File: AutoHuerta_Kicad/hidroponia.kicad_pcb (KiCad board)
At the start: 2 copper layers, 1 part

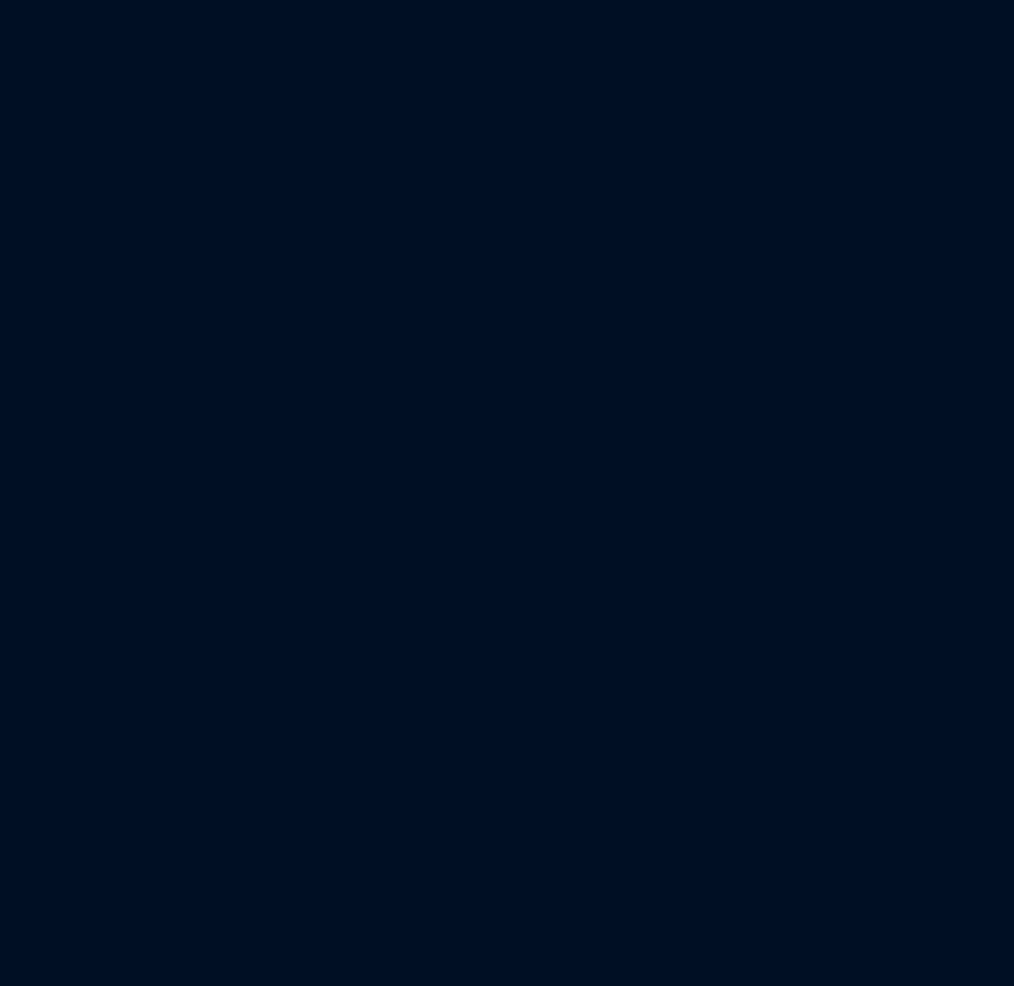
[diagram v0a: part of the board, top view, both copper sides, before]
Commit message: Actualizacion de plaqueta 17/4
agregue el control del ventilador, agregue capacito para stm32, puse huellas faltantes y conecte los pines del stm32
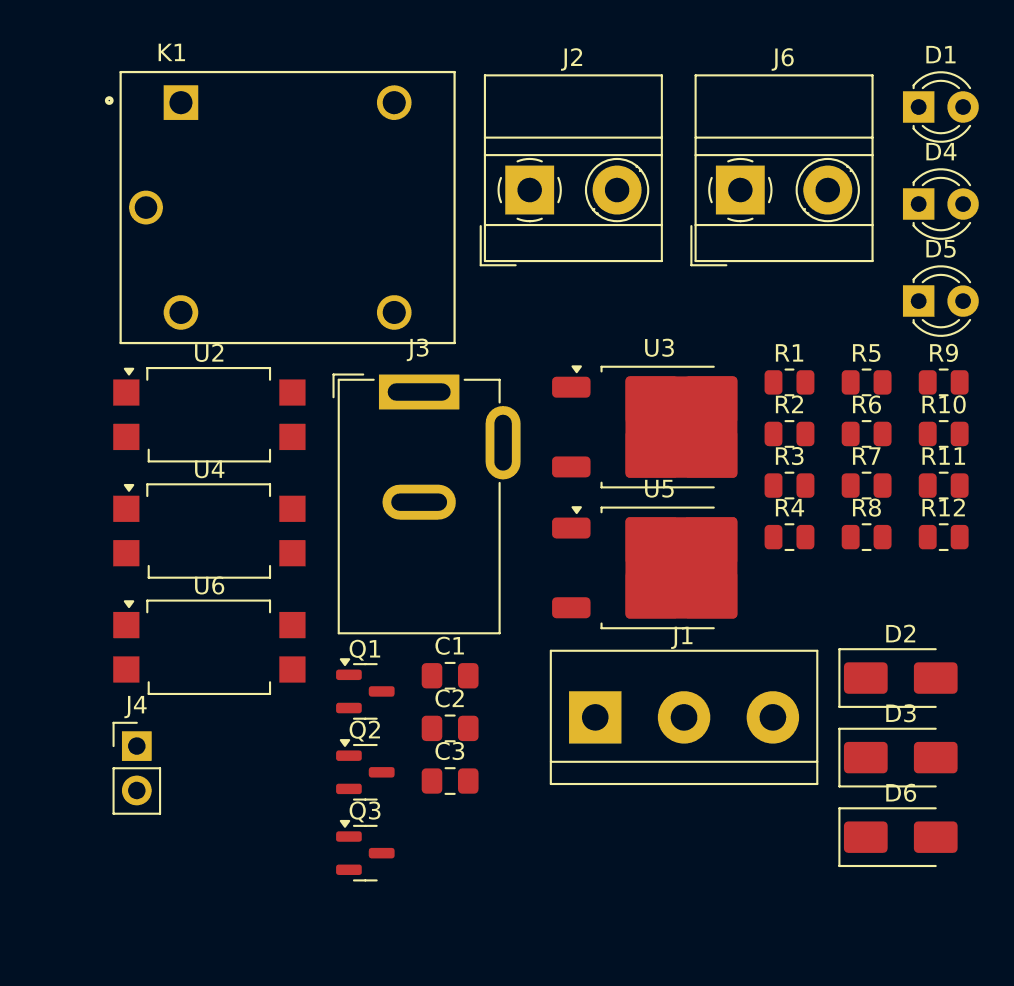
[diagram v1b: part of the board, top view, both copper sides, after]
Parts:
- added C1: 0,33uf, Capacitor_SMD:C_0805_2012Metric_Pad1.18x1.45mm_HandSolder, F.Cu at (129.3, 48.9)
- added C2: 0,1uf, Capacitor_SMD:C_0805_2012Metric_Pad1.18x1.45mm_HandSolder, F.Cu at (129.3, 51.9)
- added C3: 0,1uf, Capacitor_SMD:C_0805_2012Metric_Pad1.18x1.45mm_HandSolder, F.Cu at (129.3, 54.9)
- added D1: LED, LED_THT:LED_D3.0mm, F.Cu at (156.2, 16.4)
- added D2: 1N4007, Diode_SMD:D_SMA, F.Cu at (155.1, 49.0)
- added D3: 1N4007, Diode_SMD:D_SMA, F.Cu at (155.1, 53.6)
- added D4: LED, LED_THT:LED_D3.0mm, F.Cu at (156.2, 21.9)
- added D5: LED, LED_THT:LED_D3.0mm, F.Cu at (156.2, 27.5)
- added D6: 1N4007, Diode_SMD:D_SMA, F.Cu at (155.1, 58.1)
- added J1: bornera, TerminalBlock:TerminalBlock_bornier-3_P5.08mm, F.Cu at (137.7, 51.3)
- added J2: bornera, TerminalBlock_MetzConnect:TerminalBlock_MetzConnect_Type011_RT05502HBWC_1x02_P5.00mm_Horizontal, F.Cu at (133.9, 21.1)
- added J3: Barrel_Jack, Connector_BarrelJack:BarrelJack_GCT_DCJ200-10-A_Horizontal, F.Cu at (127.6, 32.7)
- added J4: pin, Connector_PinHeader_2.54mm:PinHeader_1x02_P2.54mm_Vertical, F.Cu at (111.4, 52.9)
- added J6: bornera, TerminalBlock_MetzConnect:TerminalBlock_MetzConnect_Type011_RT05502HBWC_1x02_P5.00mm_Horizontal, F.Cu at (145.9, 21.1)
- added K1: RELAY, SRD-05VDC-SL-C:RELAY_SRD-05VDC-SL-C, F.Cu at (120.1, 22.1)
- added Q1: BC817, Package_TO_SOT_SMD:SOT-23, F.Cu at (124.5, 49.8)
- added Q2: BS170F, Package_TO_SOT_SMD:SOT-23, F.Cu at (124.5, 54.4)
- added Q3: BC817, Package_TO_SOT_SMD:SOT-23, F.Cu at (124.5, 59.1)
- added R1: 330Ω, Resistor_SMD:R_0805_2012Metric, F.Cu at (148.8, 32.1)
- added R10: 1kΩ, Resistor_SMD:R_0805_2012Metric, F.Cu at (157.6, 35.1)
- added R11: 10kΩ, Resistor_SMD:R_0805_2012Metric, F.Cu at (157.6, 38.0)
- added R12: 330Ω, Resistor_SMD:R_0805_2012Metric, F.Cu at (157.6, 41.0)
- added R2: 1kΩ, Resistor_SMD:R_0805_2012Metric, F.Cu at (148.8, 35.1)
- added R3: 10kΩ, Resistor_SMD:R_0805_2012Metric, F.Cu at (148.8, 38.0)
- added R4: 330Ω, Resistor_SMD:R_0805_2012Metric, F.Cu at (148.8, 41.0)
- added R5: 330Ω, Resistor_SMD:R_0805_2012Metric, F.Cu at (153.2, 32.1)
- added R6: 330Ω, Resistor_SMD:R_0805_2012Metric, F.Cu at (153.2, 35.1)
- added R7: 10kΩ, Resistor_SMD:R_0805_2012Metric, F.Cu at (153.2, 38.0)
- added R8: 330Ω, Resistor_SMD:R_0805_2012Metric, F.Cu at (153.2, 41.0)
- added R9: 330Ω, Resistor_SMD:R_0805_2012Metric, F.Cu at (157.6, 32.1)
- added U2: PC817, Package_SO:SSO-4_6.7x5.1mm_P2.54mm_Clearance8mm, F.Cu at (115.6, 34.0)
- added U3: L7805, Package_TO_SOT_SMD:TO-252-2, F.Cu at (141.3, 34.7)
- added U4: PC817, Package_SO:SSO-4_6.7x5.1mm_P2.54mm_Clearance8mm, F.Cu at (115.6, 40.6)
- added U5: L7805, Package_TO_SOT_SMD:TO-252-2, F.Cu at (141.3, 42.8)
- added U6: PC817, Package_SO:SSO-4_6.7x5.1mm_P2.54mm_Clearance8mm, F.Cu at (115.6, 47.3)
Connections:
- U1 pad 18: unconnected-(U1-5V-Pad18) -> +5V1
- U1 pad 19: unconnected-(U1-GND-Pad19) -> GND
- U1 pad 25: unconnected-(U1-A0-Pad25) -> LED
- U1 pad 26: unconnected-(U1-A1-Pad26) -> BOMBA
- U1 pad 27: unconnected-(U1-A2-Pad27) -> FAN
- U1 pad 39: unconnected-(U1-GND-Pad39) -> GND
- U1 pad 40: unconnected-(U1-GND-Pad40) -> GND

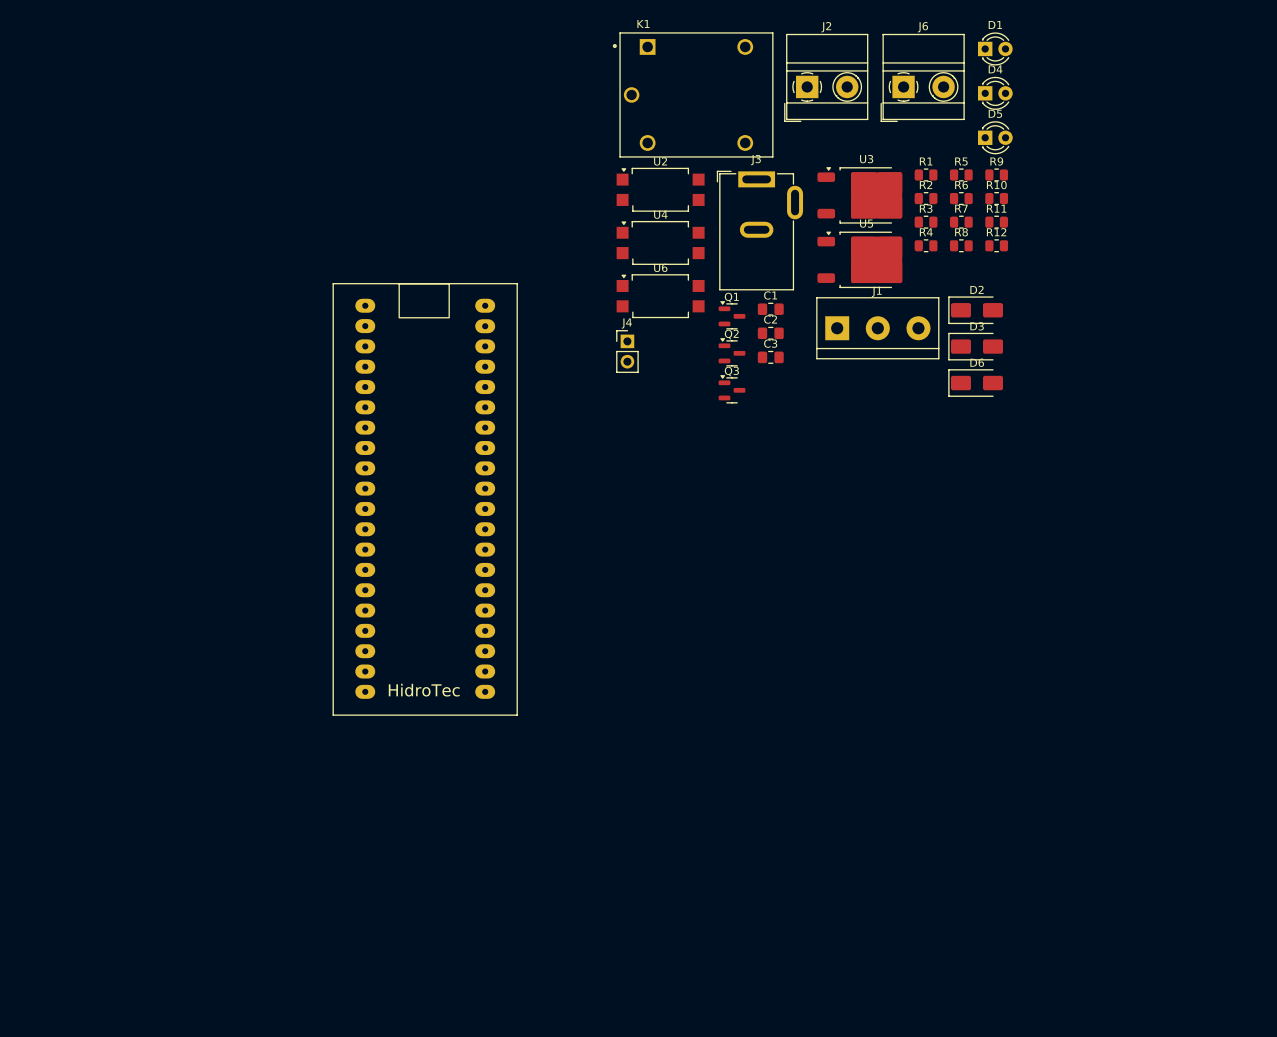
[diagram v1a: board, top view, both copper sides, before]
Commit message: Esquematico terminado
Terminamos de corregir y agregar cosas al esquematico y empezamos a acomodar los componentes en el pcb
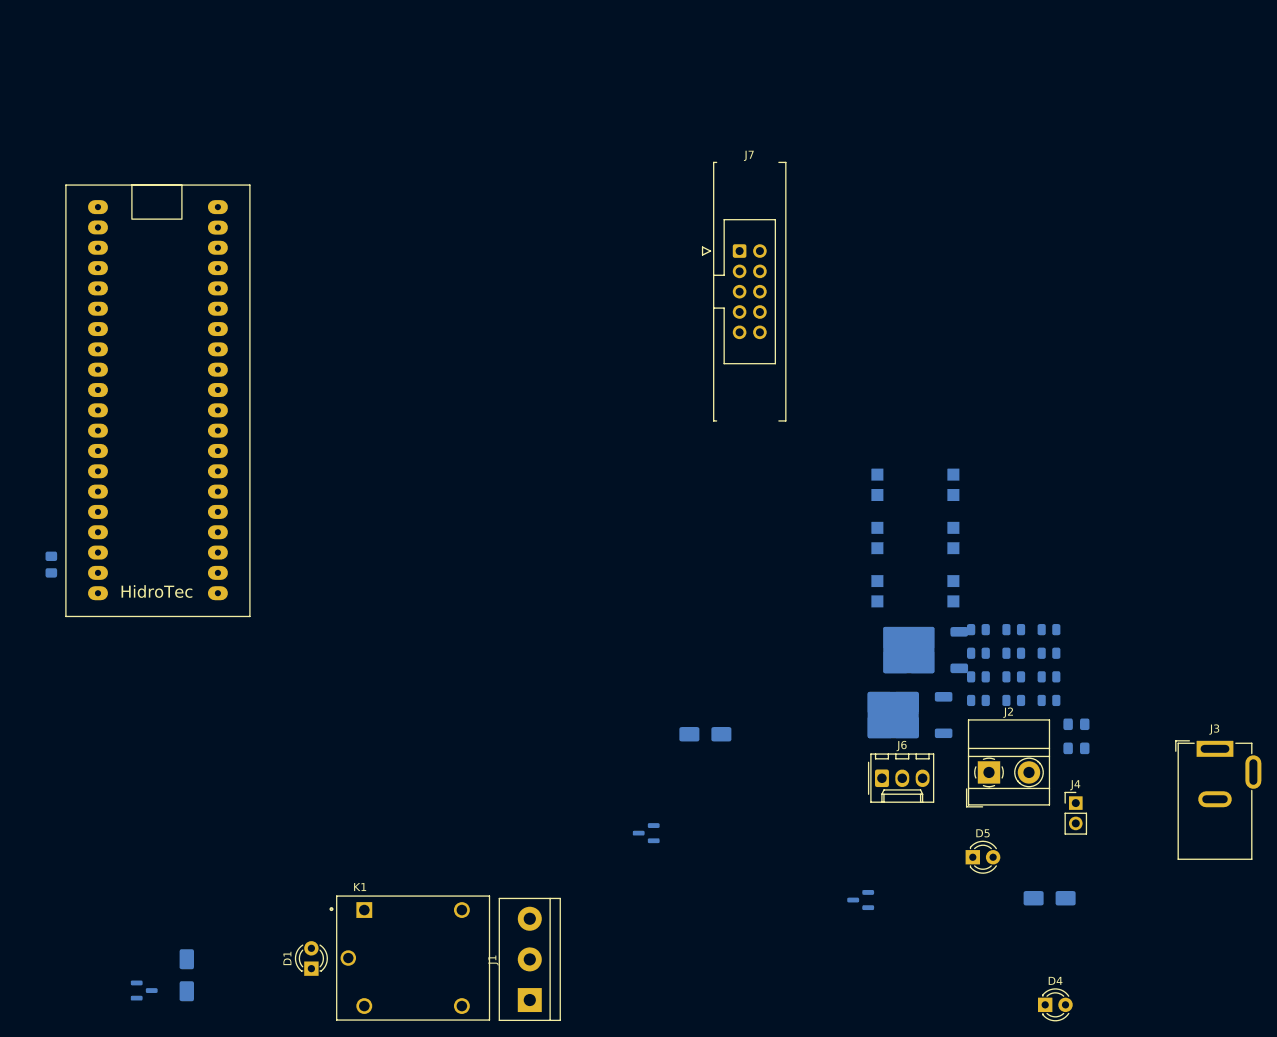
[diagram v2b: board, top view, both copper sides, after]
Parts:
- added J7: Pin, Connector_IDC:IDC-Header_2x05-1MP_P2.54mm_Latch6.5mm_Vertical, F.Cu at (125.5, 41.6)
- C1, C2, C3, D2, D3, D6, Q1, Q2, Q3, R1, R10, R11, R12, R2, R3, R4, R5, R6, R7, R8, R9, U2, U3, U4, U5, U6: moved to B.Cu
- J6: value bornera -> Pin; footprint TerminalBlock_MetzConnect:TerminalBlock_MetzConnect_Type011_RT05502HBWC_1x02_P5.00mm_Horizontal -> Connector_Molex:Molex_KK-254_AE-6410-03A_1x03_P2.54mm_Vertical
- U1: footprint huella de stm32:stm32 -> Huellas:stm32
- moved D1 142.5 mm to (71.9, 131.3), turned to 90 degrees
- moved D2 129.1 mm to (56.4, 132.2), turned to -90 degrees
- moved D4 114.2 mm to (163.7, 135.9)
- moved K1 113.5 mm to (84.6, 130.0)
- moved Q1 111.8 mm to (51.0, 134.1)
- moved C3 93.6 mm to (39.4, 80.8), turned to -90 degrees
- moved J1 92.3 mm to (99.2, 135.3), turned to 90 degrees
- moved J3 91.4 mm to (184.9, 103.9)
- moved D5 89.9 mm to (154.6, 117.4)
- moved J2 88.6 mm to (156.6, 106.8)
- moved J6 86.5 mm to (143.2, 107.6)
- moved J4 80.4 mm to (167.5, 110.7)
- moved Q2 70.2 mm to (140.6, 122.8), turned to 180 degrees
- moved D3 69.5 mm to (164.2, 122.5), turned to 180 degrees
- moved C1 64.4 mm to (167.6, 100.8), turned to 180 degrees
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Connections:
- J6 pad 1: +12V -> Net-(D5-K)
- J6 pad 2: Net-(D5-K) -> VEL
- R1 pad 1: LED -> LED & FAN
- R9 pad 1: FAN -> LED & FAN
- U1 pad 25: LED -> LED & FAN
- U1 pad 27: FAN -> VEL
- U1 pad 28: unconnected-(U1-A3-Pad28) -> A3
- U1 pad 29: unconnected-(U1-A4-Pad29) -> A4
- U1 pad 30: unconnected-(U1-A5-Pad30) -> A5
- U1 pad 31: unconnected-(U1-A6-Pad31) -> A6
- U1 pad 32: unconnected-(U1-A7-Pad32) -> A7
- U1 pad 33: unconnected-(U1-B0-Pad33) -> B0
- U1 pad 34: unconnected-(U1-B1-Pad34) -> B1

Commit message: PCB
Acomodamos un poco el PCB y cambiamos pines de lugar
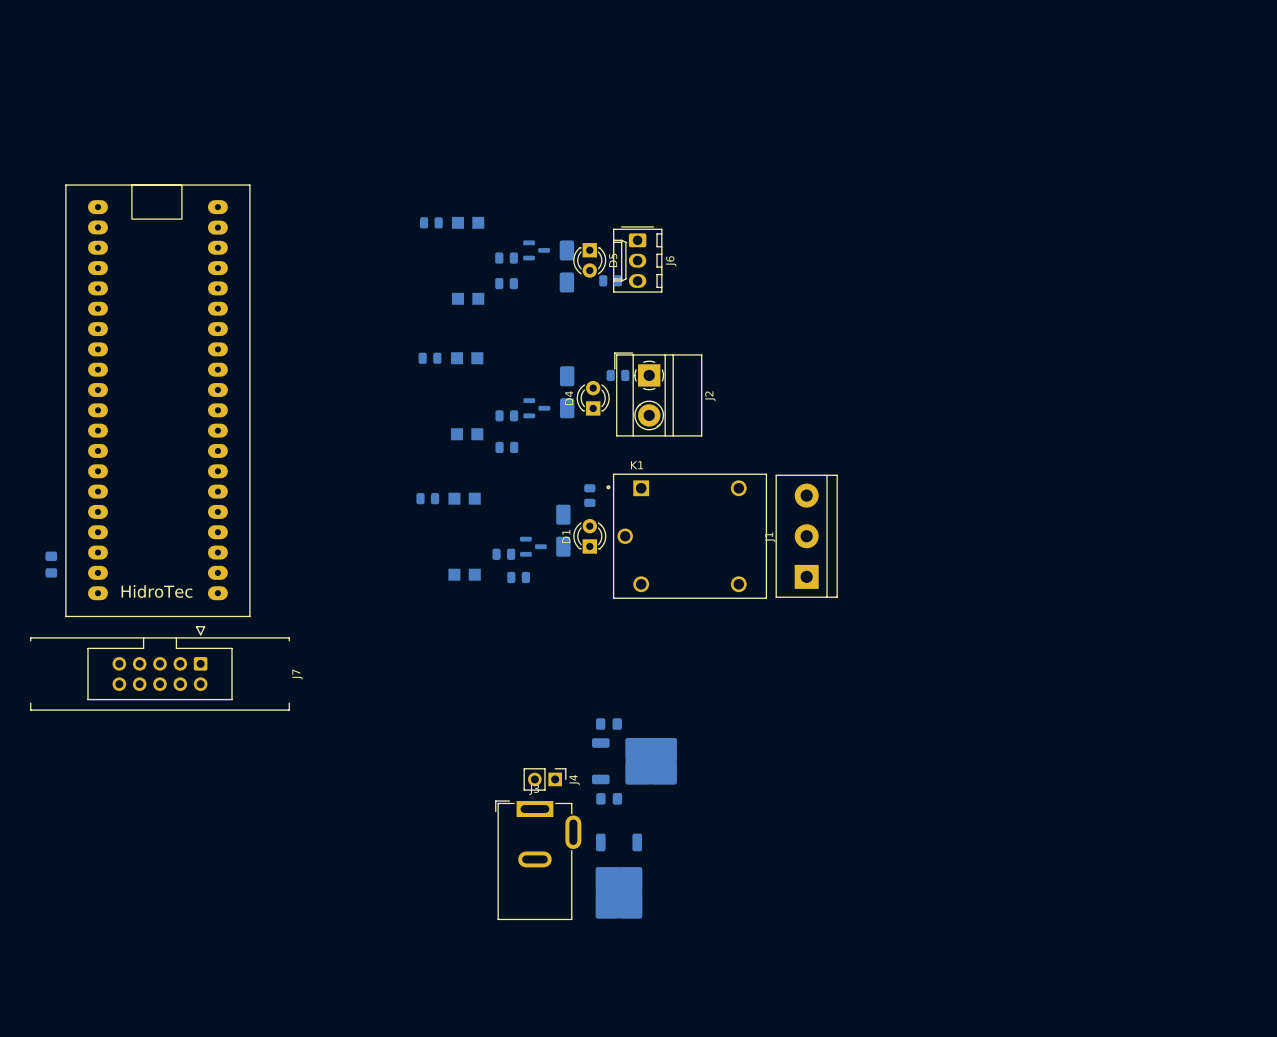
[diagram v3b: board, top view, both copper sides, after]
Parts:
- R12: value 330Ω -> 1kΩ
- moved D4 93.5 mm to (107.2, 61.3), turned to 90 degrees
- moved R9 92.4 mm to (86.9, 38.1), turned to 0 degrees
- moved D5 89.7 mm to (106.7, 41.5), turned to -90 degrees
- moved D3 87.4 mm to (103.9, 59.3), turned to -90 degrees
- moved J3 85.3 mm to (99.9, 111.4)
- moved J7 84.9 mm to (58.1, 93.2), turned to -90 degrees
- moved R10 83.9 mm to (96.3, 42.5), turned to 0 degrees
- moved R11 83.7 mm to (96.3, 45.7), turned to 0 degrees
- moved R5 80.5 mm to (86.8, 55.0), turned to 0 degrees
- moved R12 75.9 mm to (109.3, 45.4), turned to 0 degrees
- moved Q3 74.1 mm to (100.1, 41.6), turned to 0 degrees
- moved J6 73.9 mm to (112.7, 40.3), turned to -90 degrees
- moved Q1 73.8 mm to (99.7, 78.6)
- moved Q2 73.6 mm to (100.1, 61.3), turned to 0 degrees
- moved D2 72.8 mm to (103.4, 76.6)
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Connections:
- J7 pad 1: +12V -> GND
- J7 pad 2: +5V -> +12V
- J7 pad 3: GND -> +5V
